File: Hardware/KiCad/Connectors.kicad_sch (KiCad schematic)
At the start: 50 parts

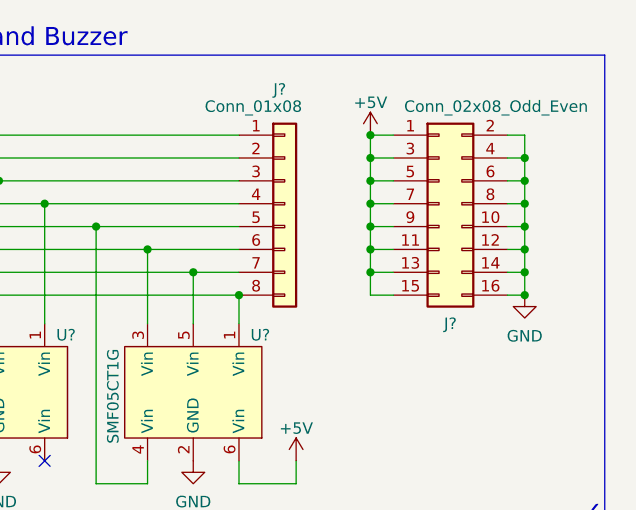
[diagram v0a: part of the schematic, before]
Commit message: Added a footprint for an optional VBAT->5V regulator
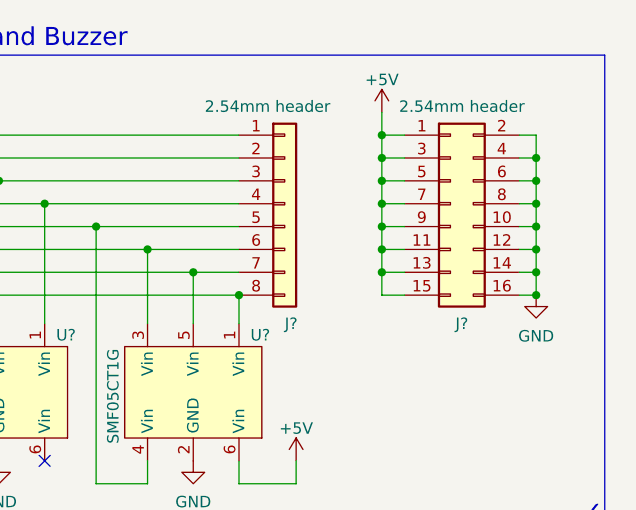
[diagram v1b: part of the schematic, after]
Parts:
- J?: value Conn_02x08_Odd_Even -> 2.54mm header
- J?: value Conn_01x08 -> 2.54mm header
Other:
- moved on the sheet: J?

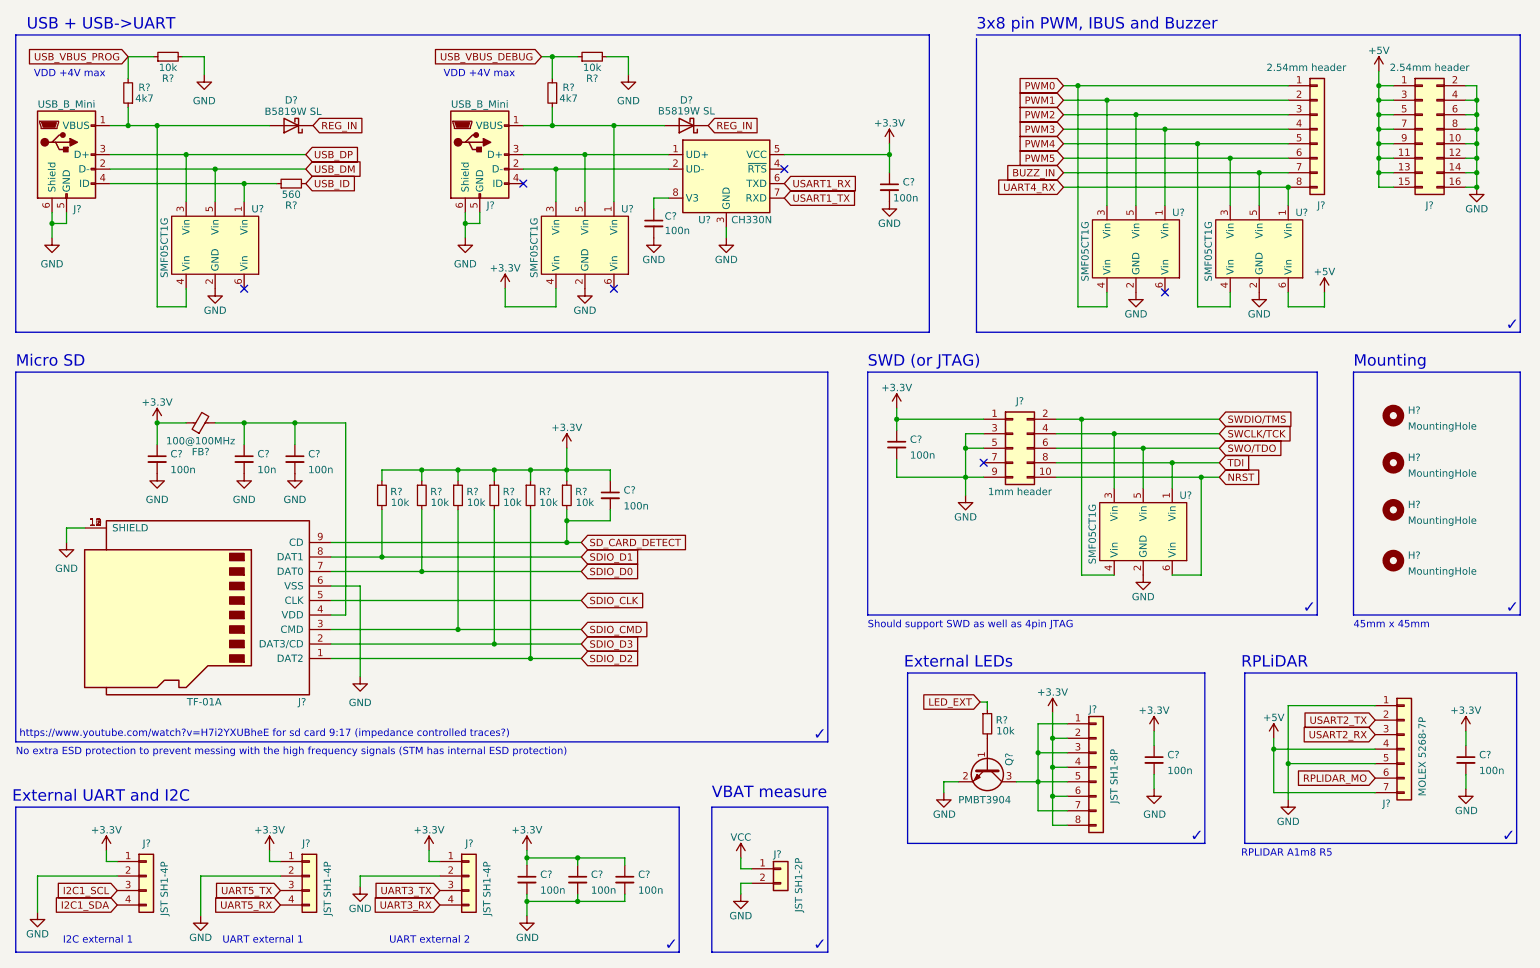
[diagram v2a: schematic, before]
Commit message: Fixed ERC errors
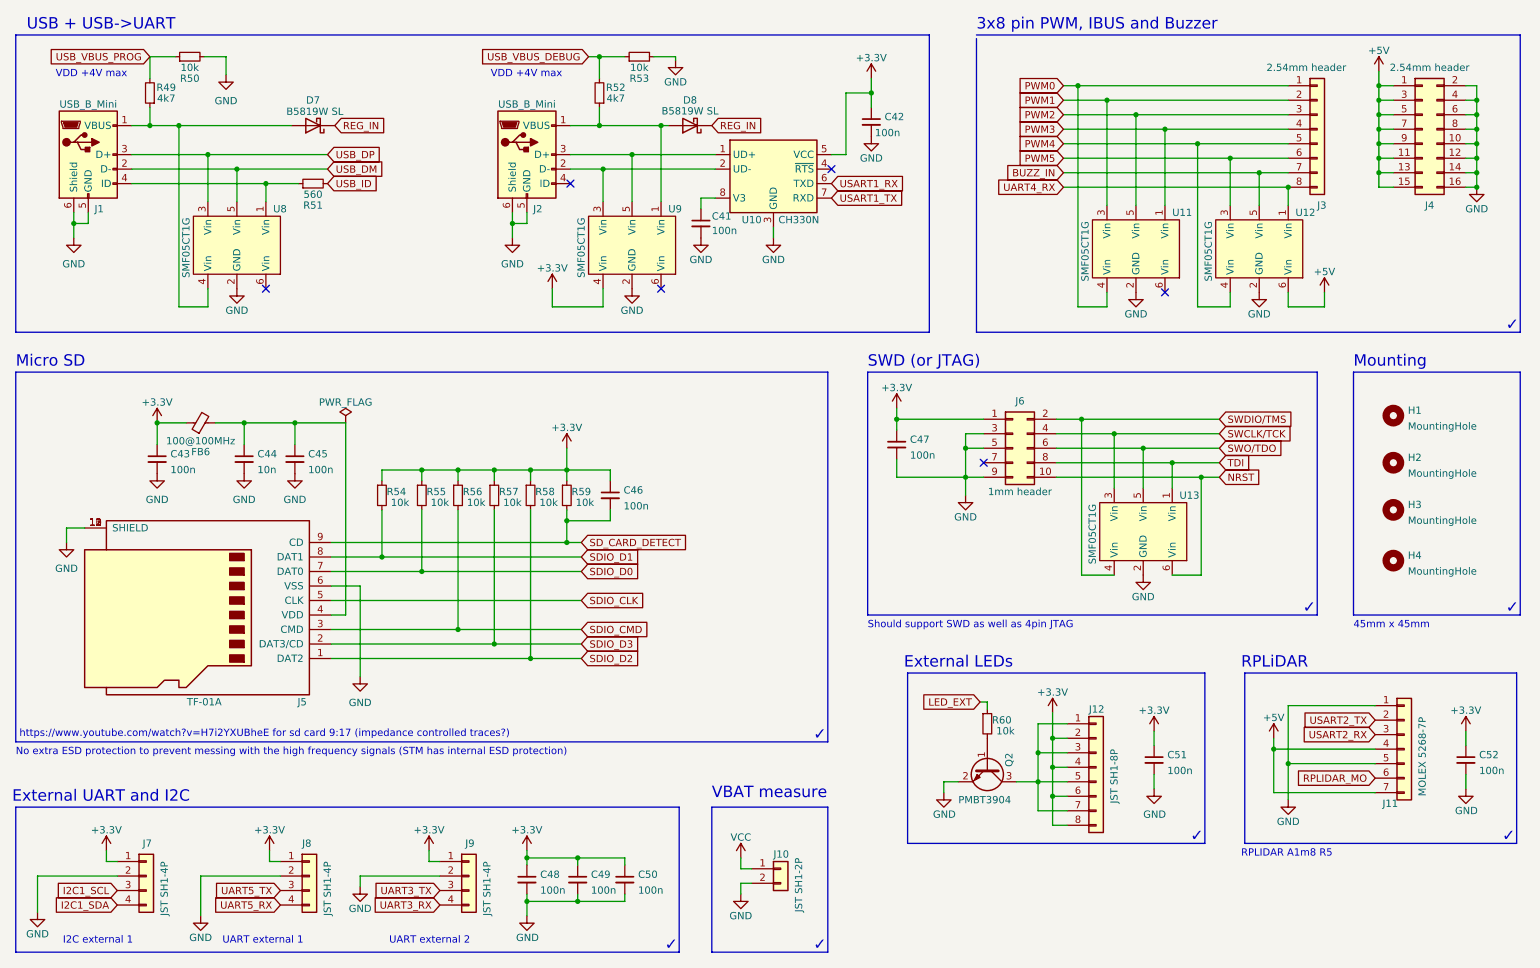
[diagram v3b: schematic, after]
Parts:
- removed J?: USB_B_Mini, Connector_USB:USB_Mini-B_Wuerth_65100516121_Horizontal, symbol Connector:USB_B_Mini
- added J2: USB_B_Mini, Connector_USB:USB_Mini-B_Wuerth_65100516121_Horizontal, symbol Connector:USB_B_Mini
- gave numbers to parts that had none: 49
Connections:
- net GND: now also J2.5 (GND), J2.6 (Shield)
- net at U10.1 (UD+), U9.5 (Vin): now also J2.3 (D+)
- net at U10.2 (UD-), U9.3 (Vin): now also J2.2 (D-)
- net at D8.2 (A), R52.1, U9.1 (Vin): now also J2.1 (VBUS)
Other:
- moved on the sheet: C41, C42, D7, D8, J1, R49, R50, R51, R52, R53, U10, U8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

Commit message: Made a general PCB layout
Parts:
- added R27, R30, R31, R32, R34: 49, Resistor_SMD:R_0402_1005Metric, symbol Device:R_Small
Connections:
- net +3V3: now also U9.3 (Vin); no longer C52.1, U9.4 (Vin)
- net +5V: now also C52.1, U11.6 (Vin), U12.4 (Vin); no longer U12.6 (Vin)
- net BUZZ_IN: now also U12.6 (Vin); no longer U12.5 (Vin)
- net NRST: now also U13.1 (Vin), R34.2; no longer J6.10 (Pin_10), U13.6 (Vin)
- net PWM0: now also U11.5 (Vin); no longer U11.4 (Vin)
- net PWM1: now also U11.4 (Vin); no longer U11.3 (Vin)
- net PWM2: now also U11.3 (Vin); no longer U11.5 (Vin)
- net PWM4: now also U12.3 (Vin); no longer U12.4 (Vin)
- net PWM5: now also U12.1 (Vin); no longer U12.3 (Vin)
- net SWCLK/TCK: now also U13.4 (Vin), R30.2; no longer J6.4 (Pin_4), U13.3 (Vin)
- net SWDIO/TMS: now also U13.3 (Vin), R27.2; no longer J6.2 (Pin_2), U13.4 (Vin)
- net SWO/TDO: now also R31.2; no longer J6.6 (Pin_6)
- net TDI: now also U13.6 (Vin), R32.2; no longer J6.8 (Pin_8), U13.1 (Vin)
- net UART4_RX: now also U12.5 (Vin); no longer U12.1 (Vin)
- net USB_DM: now also U8.6 (Vin); no longer U8.5 (Vin)
- net USB_DP: now also U8.1 (Vin); no longer U8.3 (Vin)
- net at J2.3 (D+), U10.1 (UD+): now also U9.4 (Vin); no longer U9.5 (Vin)
- net at J2.2 (D-), U10.2 (UD-): now also U9.5 (Vin); no longer U9.3 (Vin)
- net at D8.2 (A), J2.1 (VBUS), R52.1: now also U9.6 (Vin); no longer U9.1 (Vin)
- net at J1.4 (ID), R51.1: now also U8.3 (Vin); no longer U8.1 (Vin)
- net at D7.2 (A), J1.1 (VBUS), R49.1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: now also U8.5 (Vin)
- new net: J6.6 (Pin_6), R31.1
- new net: J6.10 (Pin_10), R34.1
- new net: J6.2 (Pin_2), R27.1
- new net: J6.4 (Pin_4), R30.1
- new net: J6.8 (Pin_8), R32.1
- no-connect marks 6 -> 4
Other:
- moved on the sheet: C47, J3, J6, U12

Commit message: Routing finished
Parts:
- J3: footprint Connector_PinHeader_2.54mm:PinHeader_1x08_P2.54mm_Vertical -> flightController:PinHeader_1x08_P2.54mm_Vertical_lessSilk
- J4: footprint Connector_PinHeader_2.54mm:PinHeader_2x08_P2.54mm_Horizontal -> flightController:PinHeader_2x08_P2.54mm_Horizontal_lessSilk
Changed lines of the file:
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@@
     (property "Reference" "J4" (id 0) (at 262.255 48.895 0))
     (property "Value" "2.54mm header" (id 1) (at 262.255 24.765 0))
-    (property "Footprint" "Connector_PinHeader_2.54mm:PinHeader_2x08_P2.54mm_Horizontal" (id 2) (at 260.985 35.56 0)
+    (property "Footprint" "flightController:PinHeader_2x08_P2.54mm_Horizontal_lessSilk" (id 2) (at 260.985 35.56 0)
       (effects (font (size 1.27 1.27)) hide)
     )
@@
       (effects (font (size 1.27 1.27)) (justify left))
     )
-    (property "Footprint" "Connector_PinHeader_2.54mm:PinHeader_1x08_P2.54mm_Vertical" (id 2) (at 246.38 35.56 0)
+    (property "Footprint" "flightController:PinHeader_1x08_P2.54mm_Vertical_lessSilk" (id 2) (at 246.38 35.56 0)
       (effects (font (size 1.27 1.27)) hide)
     )

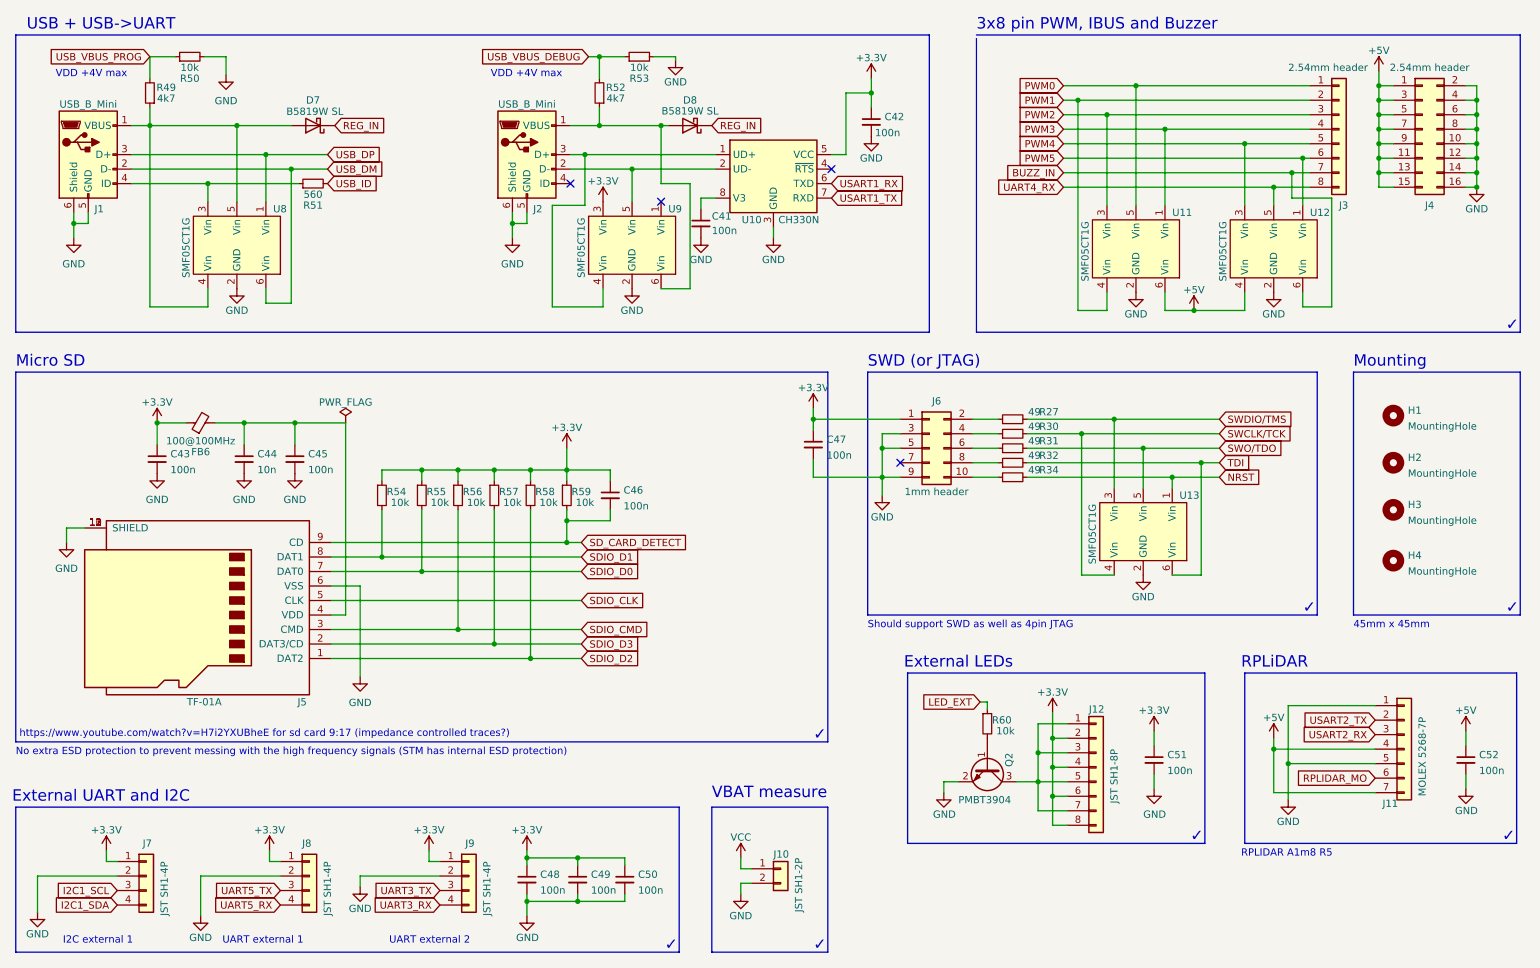
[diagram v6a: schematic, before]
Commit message: Changed the 3.3V LDO to one that supports a lower Vin so sub 5V USB supplies are less likely to pose a problem
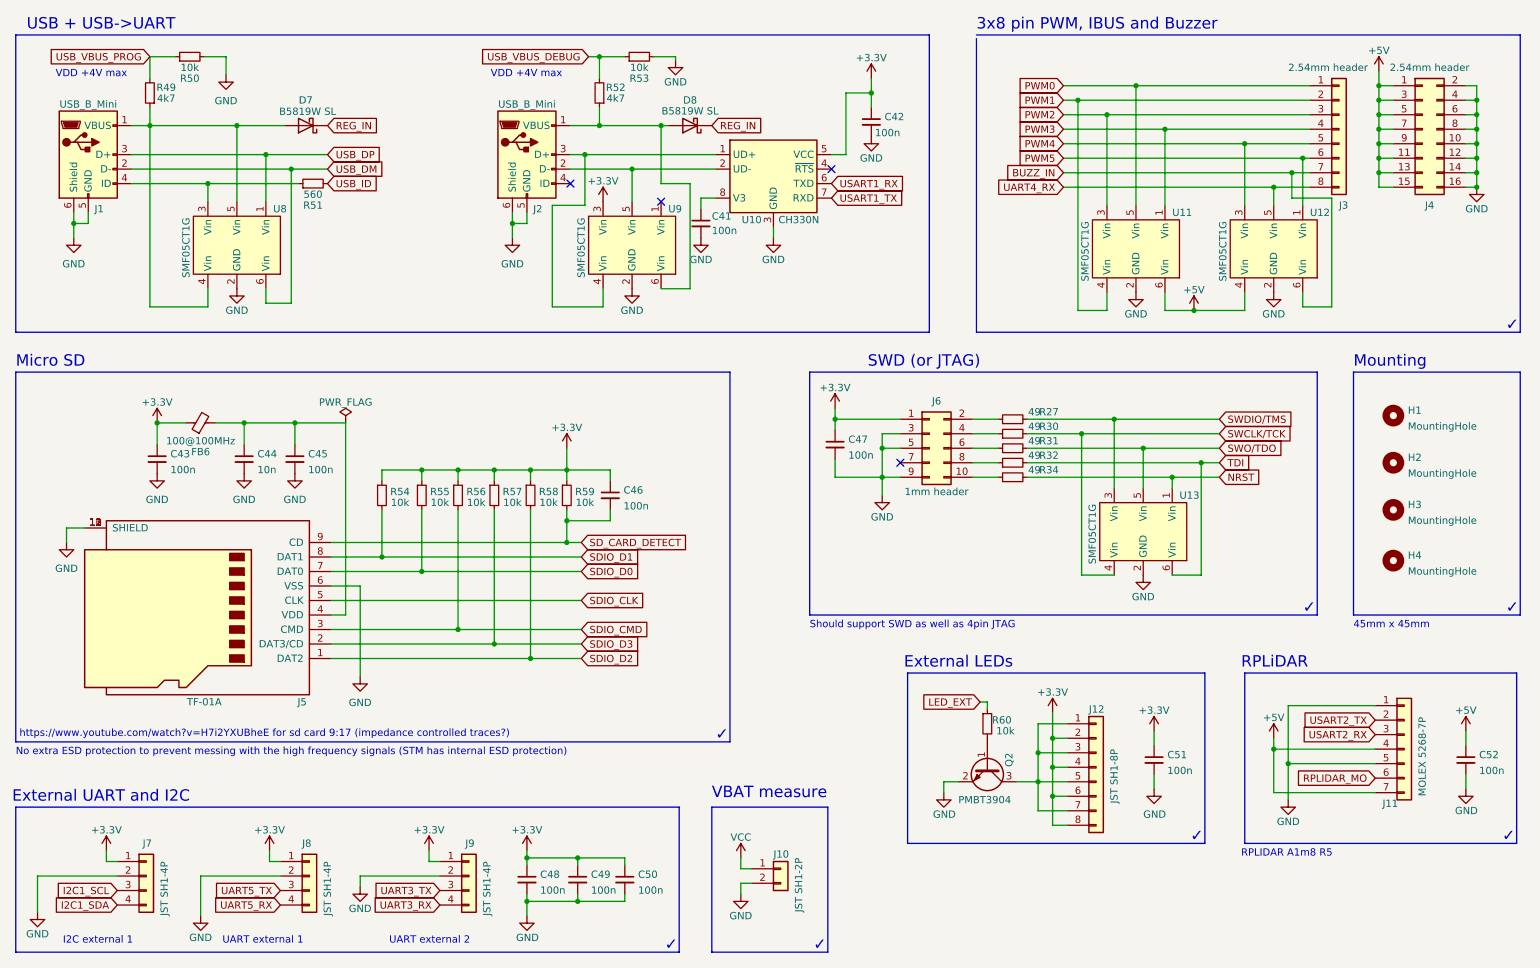
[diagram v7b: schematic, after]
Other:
- moved on the sheet: C47, D7

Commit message: SWD was 1mm pitch and needed to be 1.27 mm
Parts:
- J6: footprint Connector_PinHeader_1.00mm:PinHeader_2x05_P1.00mm_Vertical_SMD -> Connector_PinHeader_1.27mm:PinHeader_2x05_P1.27mm_Vertical_SMD
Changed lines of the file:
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@@
     (property "Reference" "J6" (id 0) (at 175.895 83.185 0))
     (property "Value" "1mm header" (id 1) (at 175.895 99.06 0))
-    (property "Footprint" "Connector_PinHeader_1.00mm:PinHeader_2x05_P1.00mm_Vertical_SMD" (id 2) (at 174.625 91.44 0)
+    (property "Footprint" "Connector_PinHeader_1.27mm:PinHeader_2x05_P1.27mm_Vertical_SMD" (id 2) (at 174.625 91.44 0)
       (effects (font (size 1.27 1.27)) hide)
     )
